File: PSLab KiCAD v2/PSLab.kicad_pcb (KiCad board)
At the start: 4 copper layers, 60 x 75 mm, 146 parts, among them CON1 USB-MINI-B, P1 CONN_01X08, P10 Analog, P11 47K, P12 5V, P13 MCLR, P2 PROG, P3 DIO, P4 V+/V-, P5 sen-cap, P6 I2C, P7 NRF, P8 CONN_02X10, P9 Tx-Rx, Q1 3906, Q2 BT5551, U1 MCP2200, U10 TL082, U11 6S21, U12 6S21, U13 TL082, U14 WS2182, U15 ESP8266, U16 TL082, U17 FOX924B, U2 74HC126, U3 PIC24EP64GP204, U4 TC1240A, U5 7660, U6 LM1117-3.3, U7 LM324, U8 TL082, U9 MCP4728

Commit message: Removed extra 15pF capacitor
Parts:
- removed C10: 15pF, MyLib:C_0805

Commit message: Added gitignore
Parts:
- removed C8: 15pF, MyLib:C_0805
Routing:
- net GND: track 149.2 -> 146.2 mm
- net 12MHz: track 49.9 -> 49.0 mm
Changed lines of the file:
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@@
 (kicad_pcb (version 4) (host pcbnew 4.0.6-e0-6349~53~ubuntu16.04.1)
   (general
-    (links 372)
+    (links 370)
     (no_connects 23)
     (area 94.02061 24.635323 178.2708 101.653201)
     (thickness 1.6)
     (drawings 65)
-    (tracks 1372)
+    (tracks 1371)
     (zones 0)
-    (modules 145)
+    (modules 144)
     (nets 145)
   )
@@
     )
   )
-  (module MyLib:C_0805 (layer F.Cu-L1)
-    (at 153.63 63.0938 90)
-    (descr "Capacitor SMD 0805, reflow soldering, AVX (see smccp.pdf), AVX (see smccp.pdf)")
-    (tags "capacitor 0805")
-    (attr smd)
-    (fp_text reference C8 (at 0.25 2.71 90) (layer F.SilkS)
-      (effects (font (size 0.8 0.8) (thickness 0.1)))
-    )
-    (fp_text value 15pF (at 0.22 1.64 90) (layer F.SilkS)
-      (effects (font (size 0.8 0.8) (thickness 0.1)))
-    )
-    (fp_line (start 0.5 -0.85) (end -0.5 -0.85) (layer F.SilkS) (width 0.15))
-    (fp_line (start -0.5 0.85) (end 0.5 0.85) (layer F.SilkS) (width 0.15))
-    (pad 1 smd rect (at -1 0 90) (size 1 1.3) (layers F.Cu-L1 F.Paste F.Mask)
-      (net 1 GND))
-    (pad 2 smd rect (at 1 0 90) (size 1 1.3) (layers F.Cu-L1 F.Paste F.Mask)
-      (net 95 12MHz))
-    (model Capacitors_SMD/C_0805N.wrl
-      (at (xyz 0 0 0))
-      (scale (xyz 1 1 1))
-      (rotate (xyz 0 0 0))
-    )
-  )
   (module MyLib:C_0805 (layer B.Cu-L4)
     (at 121.1 55.55 270)
@@
     (effects (font (size 1 1) (thickness 0.1)))
   )
-  (segment (start 153.1272 64.5966) (end 153.63 64.0938) (width 0.3048) (layer F.Cu-L1) (net 1))
-  (segment (start 150.8176 64.5966) (end 153.1272 64.5966) (width 0.3048) (layer F.Cu-L1) (net 1))
   (segment (start 145.3013 68.3999) (end 142.165 68.3999) (width 0.3048) (layer F.Cu-L1) (net 1))
   (segment (start 147.3054 66.3958) (end 145.3013 68.3999) (width 0.3048) (layer F.Cu-L1) (net 1))
@@
   (segment (start 142.165 73.2005) (end 142.6205 73.2005) (width 0.3048) (layer F.Cu-L1) (net 94) (status 30))
   (segment (start 142.165 73.2005) (end 142.2005 73.2005) (width 0.3048) (layer F.Cu-L1) (net 94) (status 30))
+  (segment (start 151.5218 62.5858) (end 151.6488 62.5858) (width 0.3048) (layer F.Cu-L1) (net 95))
+  (segment (start 153.63 60.6046) (end 153.63 59.8172) (width 0.3048) (layer F.Cu-L1) (net 95))
+  (segment (start 151.6488 62.5858) (end 153.63 60.6046) (width 0.3048) (layer F.Cu-L1) (net 95))
   (segment (start 143.1 34.205) (end 146.5598 34.205) (width 0.254) (layer F.Cu-L1) (net 95))
-  (segment (start 153.63 59.8172) (end 153.63 62.0938) (width 0.254) (layer F.Cu-L1) (net 95))
   (segment (start 155.4842 57.963) (end 153.63 59.8172) (width 0.254) (layer F.Cu-L1) (net 95))
   (via (at 155.4842 57.963) (size 0.9144) (drill 0.4064) (layers F.Cu-L1 B.Cu-L4) (net 95))
@@
   (segment (start 148.3722 36.0174) (end 148.3722 44.755) (width 0.254) (layer F.Cu-L1) (net 95))
   (segment (start 146.5598 34.205) (end 148.3722 36.0174) (width 0.254) (layer F.Cu-L1) (net 95))
-  (segment (start 153.138 62.5858) (end 153.63 62.0938) (width 0.3048) (layer F.Cu-L1) (net 95))
-  (segment (start 150.0486 62.5858) (end 153.138 62.5858) (width 0.3048) (layer F.Cu-L1) (net 95))
   (segment (start 148.5176 64.1168) (end 150.0486 62.5858) (width 0.3048) (layer F.Cu-L1) (net 95))
+  (segment (start 150.0486 62.5858) (end 151.5218 62.5858) (width 0.3048) (layer F.Cu-L1) (net 95))
   (segment (start 148.5176 64.5966) (end 148.5176 64.1168) (width 0.3048) (layer F.Cu-L1) (net 95))
   (segment (start 148.5176 64.5966) (end 147.4028 64.5966) (width 0.3048) (layer F.Cu-L1) (net 95))

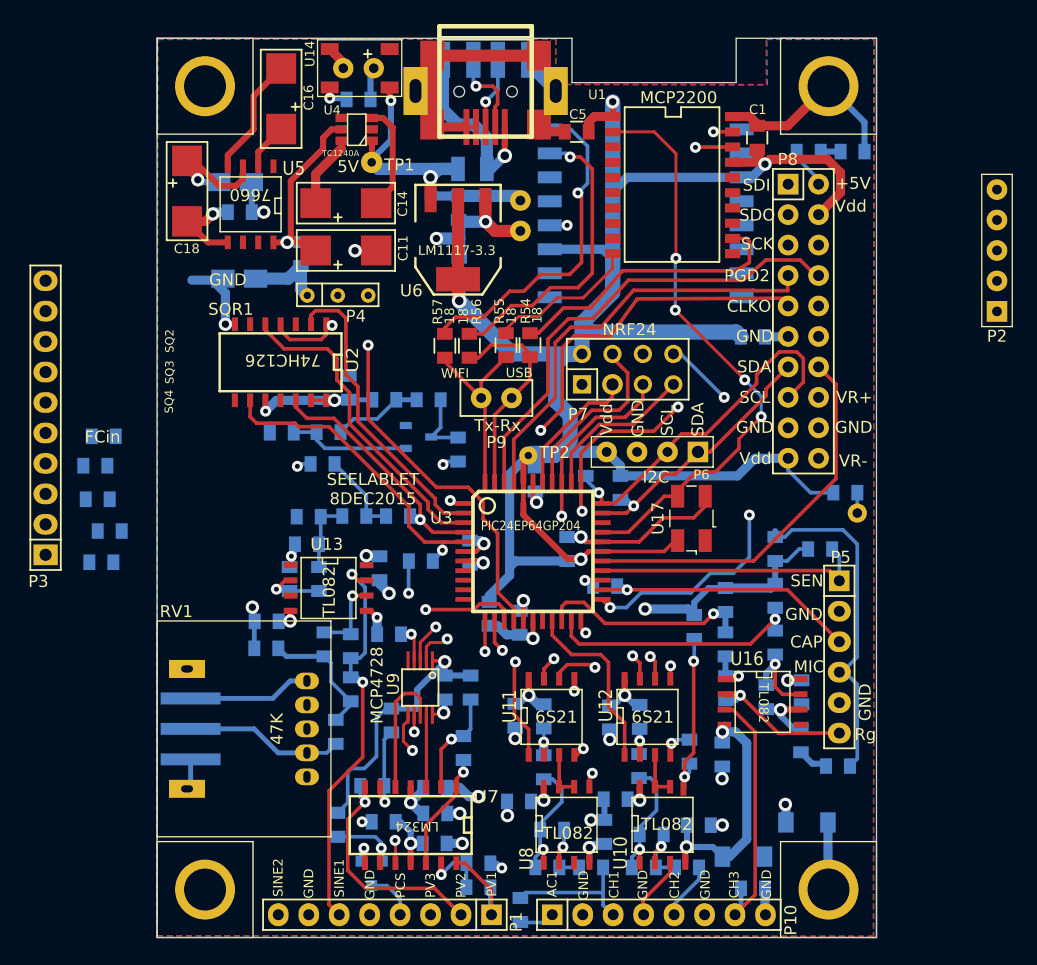
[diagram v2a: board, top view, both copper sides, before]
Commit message: DRC errors fixed in pcb layout (#18)
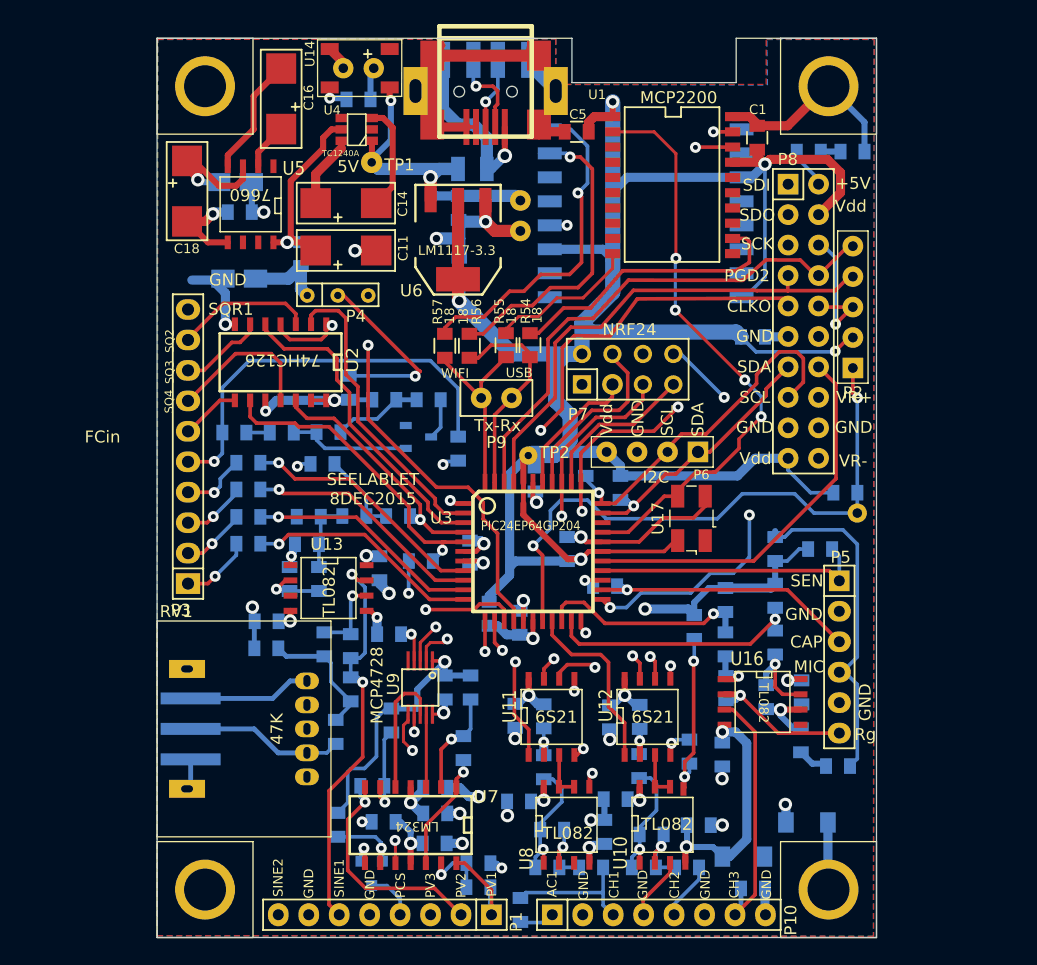
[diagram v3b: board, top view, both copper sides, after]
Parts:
- moved P2 12.9 mm to (163.1, 48.8)
- moved R6 12.8 mm to (112.7, 61.8)
- moved R7 12.6 mm to (112.7, 64.0)
- moved R9 12.4 mm to (112.7, 68.6)
- moved P3 12.1 mm to (107.7, 60.5)
- moved R8 11.6 mm to (112.7, 66.3)
- moved R51 10.9 mm to (111.5, 59.3)
- moved R49 0.07 mm to (130.2, 60.6)
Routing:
- net /MCLR: track 1.70 -> 50.4 mm, vias 0 -> 2
- net /FCin: track 0.00 -> 34.2 mm, vias 0 -> 1
- net GND: track 146.2 -> 174.1 mm, vias 25 -> 27
- net Vdd: track 188.5 -> 210.9 mm, vias 4 -> 5
- net Net-(R6-Pad2): track 0.00 -> 20.8 mm, vias 0 -> 1
- net Net-(R7-Pad2): track 0.00 -> 20.2 mm, vias 0 -> 1
- net Net-(R9-Pad2): track 0.00 -> 19.6 mm, vias 0 -> 1
- net Net-(R8-Pad2): track 0.00 -> 19.5 mm, vias 0 -> 1
- net /SQR3: track 0.00 -> 12.8 mm
- net /SQR1: track 0.00 -> 11.5 mm
- net /SQR2: track 0.00 -> 7.17 mm
- net /ID4: track 0.00 -> 5.96 mm, vias 0 -> 1
- net PGD2: track 36.8 -> 42.7 mm
- net /ID1: track 0.00 -> 5.45 mm, vias 0 -> 1
- net /ID3: track 0.00 -> 5.41 mm, vias 0 -> 1
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
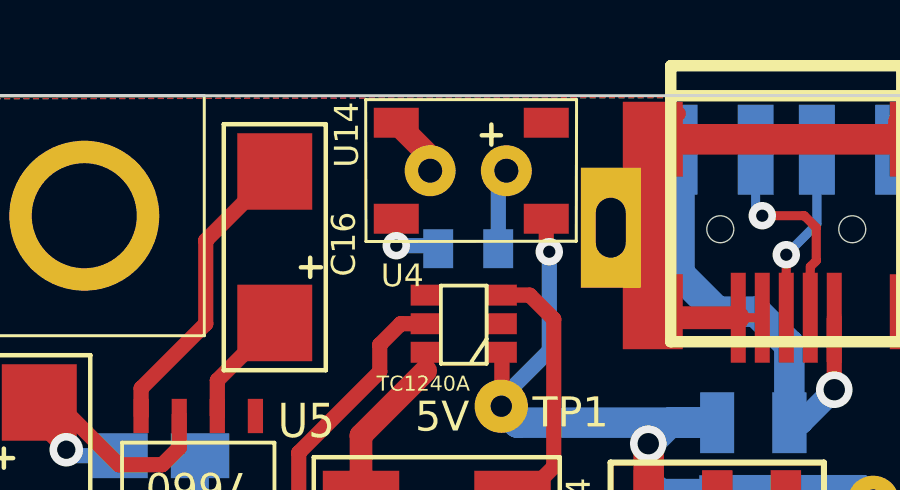
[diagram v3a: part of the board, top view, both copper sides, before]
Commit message: Fix #19: Removed redundant LED foot print
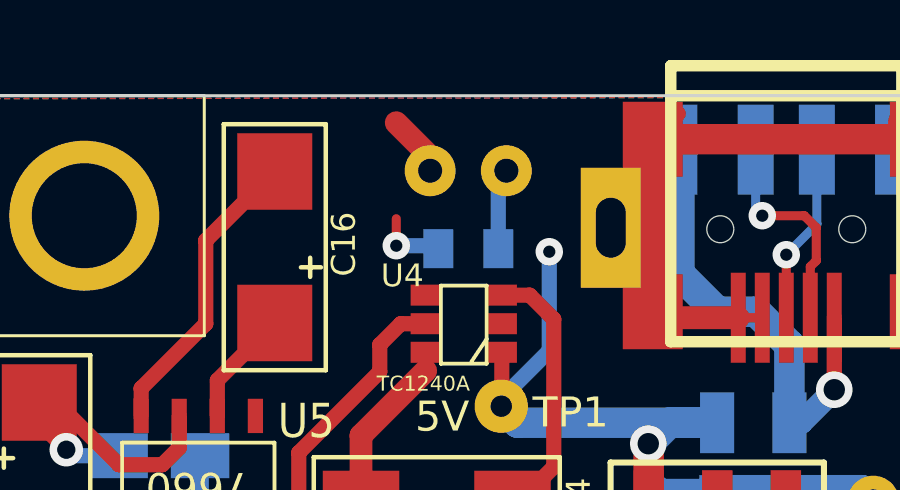
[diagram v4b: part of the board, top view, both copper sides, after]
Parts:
- removed U14: WS2182, MyLib:SM5050
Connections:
- net VUSB renamed Net-(CON1-Pad1)
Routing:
- net +5V: track 124.2 -> 123.2 mm
